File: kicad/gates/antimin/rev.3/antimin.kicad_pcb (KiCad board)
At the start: 2 copper layers, 15.2 x 7.4 mm, 6 parts, among them J1 Conn_01x03, J2 Conn_01x03, Q1 BSS8402DW, Q2 BSS8402DW

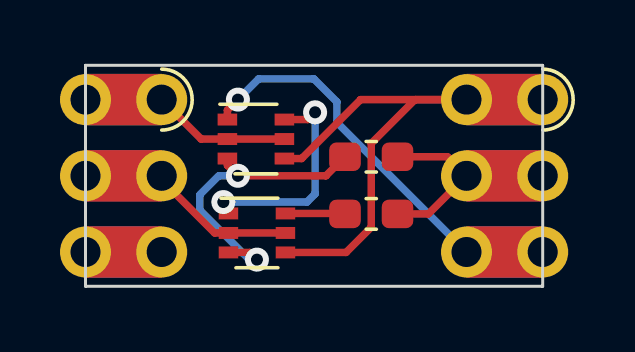
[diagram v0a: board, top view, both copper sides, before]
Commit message: updated antimin rev.3 pcb to fix board size
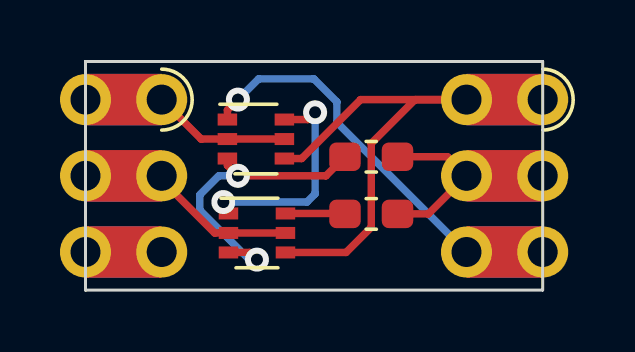
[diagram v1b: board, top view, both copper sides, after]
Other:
- board size 15.2 x 7.4 mm -> 15.2 x 7.6 mm
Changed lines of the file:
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@@
     (thickness 1.6)
     (drawings 6)
-    (tracks 58)
+    (tracks 57)
     (zones 0)
     (modules 6)
@@
     )
   )
-  (gr_line (start 95.25 55.372) (end 95.25 62.738) (layer Edge.Cuts) (width 0.1))
-  (gr_line (start 80.01 55.372) (end 95.25 55.372) (layer Edge.Cuts) (width 0.1))
-  (gr_line (start 80.01 62.738) (end 80.01 55.372) (layer Edge.Cuts) (width 0.1))
-  (gr_line (start 95.25 62.738) (end 80.01 62.738) (layer Edge.Cuts) (width 0.1))
+  (gr_line (start 95.25 55.245) (end 95.25 62.865) (layer Edge.Cuts) (width 0.1))
+  (gr_line (start 80.01 55.245) (end 95.25 55.245) (layer Edge.Cuts) (width 0.1))
+  (gr_line (start 80.01 62.865) (end 80.01 55.245) (layer Edge.Cuts) (width 0.1))
+  (gr_line (start 95.25 62.865) (end 80.01 62.865) (layer Edge.Cuts) (width 0.1))
   (gr_text rev.3 (at 87.884 61.976) (layer B.SilkS)
     (effects (font (size 1 1) (thickness 0.15)) (justify mirror))
@@
   (segment (start 83.865 57.83) (end 84.74 57.83) (width 0.25) (layer F.Cu) (net 5))
   (segment (start 82.55 56.515) (end 83.865 57.83) (width 0.25) (layer F.Cu) (net 5))
-  (segment (start 87.63 56.515) (end 87.63 56.515) (width 0.25) (layer F.Cu) (net 7))
   (segment (start 84.455 59.69) (end 84.455 59.69) (width 0.25) (layer F.Cu) (net 7))
   (segment (start 84.775 60.31) (end 84.775 60.10001) (width 0.25) (layer F.Cu) (net 7))
